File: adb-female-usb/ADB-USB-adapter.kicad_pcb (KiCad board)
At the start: 2 copper layers, 31.8 x 21.6 mm, 2 parts

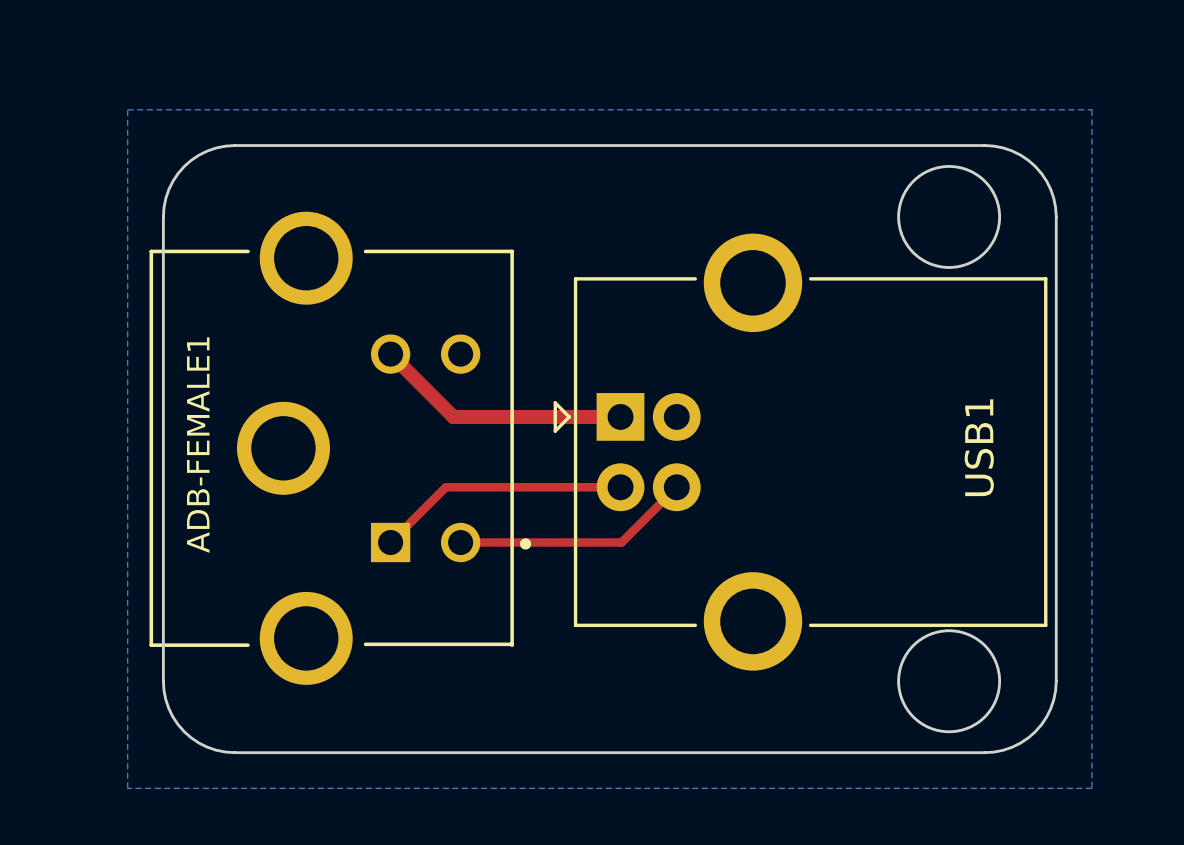
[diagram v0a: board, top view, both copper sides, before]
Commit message: switched D+/D- on USB PCB, isolated shield from ground
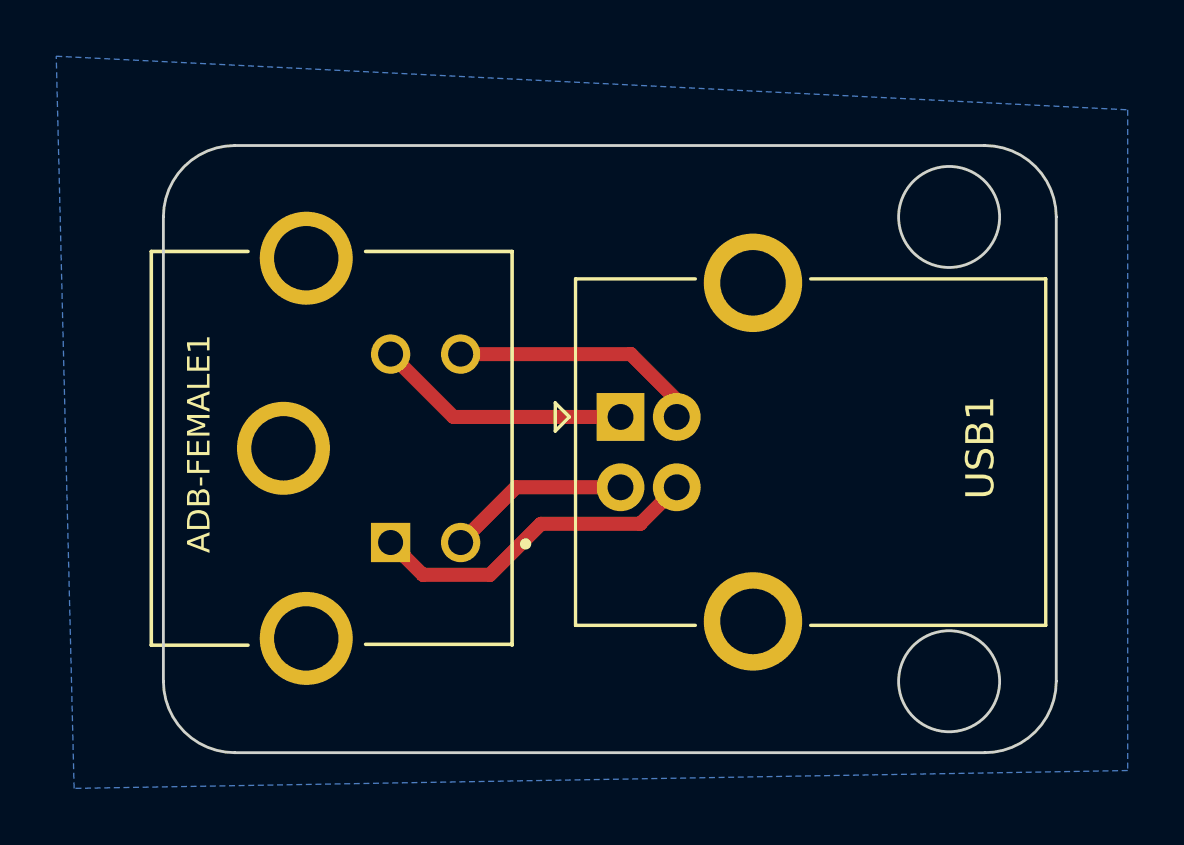
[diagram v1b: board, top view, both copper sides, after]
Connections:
- ADB-FEMALE1 pad 1: Net-(USB1-D-) -> Net-(USB1-D+)
- ADB-FEMALE1 pad 3: Net-(USB1-D+) -> Net-(USB1-D-)
- ADB-FEMALE1 pad 5: GND -> Net-(USB1-Shield)
- ADB-FEMALE1 pad 6: GND -> Net-(USB1-Shield)
- ADB-FEMALE1 pad 7: GND -> Net-(USB1-Shield)
- USB1 pad 5: GND -> Net-(USB1-Shield)
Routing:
- net GND: track 0.00 -> 8.96 mm
- net Net-(USB1-D+): track 8.50 -> 11.9 mm
- net Net-(USB1-D-): track 8.99 -> 6.50 mm
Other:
- board text added: "joanne-lab rev 2.0"
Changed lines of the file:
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@@
       (outputformat 1)
       (mirror false)
-      (drillshape 1)
+      (drillshape 0)
       (scaleselection 1)
-      (outputdirectory "")
+      (outputdirectory "../fabrication/adb-female-usb/")
     )
   )
   (net 0 "")
-  (net 1 "GND")
-  (net 2 "Net-(USB1-VBUS)")
-  (net 3 "Net-(USB1-D+)")
-  (net 4 "Net-(USB1-D-)")
+  (net 1 "Net-(USB1-VBUS)")
+  (net 2 "Net-(USB1-D+)")
+  (net 3 "Net-(USB1-D-)")
+  (net 4 "Net-(USB1-Shield)")
+  (net 5 "GND")
   (footprint "Connector_USB:USB_B_OST_USB-B1HSxx_Horizontal" (layer "F.Cu")
     (at 36.576 28.702)
@@
       (stroke (width 0.1) (type solid)) (layer "F.Fab"))
     (pad "1" thru_hole rect (at 0 0) (size 1.7 1.7) (drill 0.92) (layers "*.Cu" "*.Mask")
-      (net 2 "Net-(USB1-VBUS)") (pinfunction "VBUS") (pintype "power_out"))
+      (net 1 "Net-(USB1-VBUS)") (pinfunction "VBUS") (pintype "power_out"))
     (pad "2" thru_hole circle (at 0 2.5) (size 1.7 1.7) (drill 0.92) (layers "*.Cu" "*.Mask")
-      (net 4 "Net-(USB1-D-)") (pinfunction "D-") (pintype "bidirectional"))
+      (net 3 "Net-(USB1-D-)") (pinfunction "D-") (pintype "bidirectional"))
     (pad "3" thru_hole circle (at 2 2.5) (size 1.7 1.7) (drill 0.92) (layers "*.Cu" "*.Mask")
-      (net 3 "Net-(USB1-D+)") (pinfunction "D+") (pintype "bidirectional"))
+      (net 2 "Net-(USB1-D+)") (pinfunction "D+") (pintype "bidirectional"))
     (pad "4" thru_hole circle (at 2 0) (size 1.7 1.7) (drill 0.92) (layers "*.Cu" "*.Mask")
-      (net 1 "GND") (pinfunction "GND") (pintype "power_out"))
+      (net 5 "GND") (pinfunction "GND") (pintype "power_out"))
     (pad "5" thru_hole circle (at 4.71 -4.77) (size 3.5 3.5) (drill 2.33) (layers "*.Cu" "*.Mask")
-      (net 1 "GND") (pinfunction "Shield") (pintype "passive"))
+      (net 4 "Net-(USB1-Shield)") (pinfunction "Shield") (pintype "passive"))
     (pad "5" thru_hole circle (at 4.71 7.27) (size 3.5 3.5) (drill 2.33) (layers "*.Cu" "*.Mask")
-      (net 1 "GND") (pinfunction "Shield") (pintype "passive"))
+      (net 4 "Net-(USB1-Shield)") (pinfunction "Shield") (pintype "passive"))
     (model "${KICAD6_3DMODEL_DIR}/Connector_USB.3dshapes/USB_B_OST_USB-B1HSxx_Horizontal.wrl"
       (offset (xyz 0 0 0))
@@
       (stroke (width 0.127) (type solid)) (layer "F.Fab"))
     (pad "1" thru_hole rect (at -3.35 0 90) (size 1.398 1.398) (drill 0.89) (layers "*.Cu" "*.Mask")
-      (net 4 "Net-(USB1-D-)") (pinfunction "1") (pintype "passive") (solder_mask_margin 0.102))
+      (net 2 "Net-(USB1-D+)") (pinfunction "1") (pintype "passive") (solder_mask_margin 0.102))
     (pad "2" thru_hole circle (at 3.35 0 90) (size 1.398 1.398) (drill 0.89) (layers "*.Cu" "*.Mask")
-      (net 2 "Net-(USB1-VBUS)") (pinfunction "2") (pintype "passive") (solder_mask_margin 0.102))
+      (net 1 "Net-(USB1-VBUS)") (pinfunction "2") (pintype "passive") (solder_mask_margin 0.102))
     (pad "3" thru_hole circle (at -3.35 2.49 90) (size 1.398 1.398) (drill 0.89) (layers "*.Cu" "*.Mask")
-      (net 3 "Net-(USB1-D+)") (pinfunction "3") (pintype "passive") (solder_mask_margin 0.102))
+      (net 3 "Net-(USB1-D-)") (pinfunction "3") (pintype "passive") (solder_mask_margin 0.102))
     (pad "4" thru_hole circle (at 3.35 2.49 90) (size 1.398 1.398) (drill 0.89) (layers "*.Cu" "*.Mask")
-      (net 1 "GND") (pinfunction "4") (pintype "passive") (solder_mask_margin 0.102))
+      (net 5 "GND") (pinfunction "4") (pintype "passive") (solder_mask_margin 0.102))
     (pad "5" thru_hole circle (at 0 -3.81 90) (size 3.306 3.306) (drill 2.29) (layers "*.Cu" "*.Mask")
-      (net 1 "GND") (pinfunction "SH") (pintype "passive") (solder_mask_margin 0.102))
+      (net 4 "Net-(USB1-Shield)") (pinfunction "SH") (pintype "passive") (solder_mask_margin 0.102))
     (pad "6" thru_hole circle (at 6.76 -3 90) (size 3.306 3.306) (drill 2.29) (layers "*.Cu" "*.Mask")
-      (net 1 "GND") (pinfunction "SH") (pintype "passive") (solder_mask_margin 0.102))
+      (net 4 "Net-(USB1-Shield)") (pinfunction "SH") (pintype "passive") (solder_mask_margin 0.102))
     (pad "7" thru_hole circle (at -6.76 -3 90) (size 3.306 3.306) (drill 2.29) (layers "*.Cu" "*.Mask")
-      (net 1 "GND") (pinfunction "SH") (pintype "passive") (solder_mask_margin 0.102))
+      (net 4 "Net-(USB1-Shield)") (pinfunction "SH") (pintype "passive") (solder_mask_margin 0.102))
   )
   (gr_circle (center 48.26 38.1) (end 49.53 39.37)
@@
   (gr_line (start 22.86 19.05) (end 49.53 19.05)
     (stroke (width 0.1) (type default)) (layer "Edge.Cuts"))
+  (gr_text "joanne-lab\nrev 2.0" (at 49.53 31.115) (layer "B.SilkS")
+    (effects (font (size 1 1) (thickness 0.15)) (justify left bottom mirror))
+  )
   (gr_text "GND" (at 30.226 25.4 -90) (layer "B.SilkS")
     (effects (font (size 1 1) (thickness 0.15)) (justify left bottom mirror))
@@
     (effects (font (size 1 1) (thickness 0.15)) (justify left bottom mirror))
   )
-  (segment (start 28.4 26.4668) (end 30.6352 28.702) (width 0.5) (layer "F.Cu") (net 2))
-  (segment (start 30.6352 28.702) (end 36.576 28.702) (width 0.5) (layer "F.Cu") (net 2))
-  (segment (start 36.6112 33.1668) (end 30.89 33.1668) (width 0.3) (layer "F.Cu") (net 3))
-  (segment (start 38.576 31.202) (end 36.6112 33.1668) (width 0.3) (layer "F.Cu") (net 3))
-  (segment (start 36.576 31.202) (end 30.3648 31.202) (width 0.3) (layer "F.Cu") (net 4))
-  (segment (start 30.3648 31.202) (end 28.4 33.1668) (width 0.3) (layer "F.Cu") (net 4))
-  (zone (net 1) (net_name "GND") (layer "B.Cu") (hatch edge 0.5)
+  (segment (start 36.576 28.702) (end 30.6352 28.702) (width 0.5) (layer "F.Cu") (net 1))
+  (segment (start 30.6352 28.702) (end 28.4 26.4668) (width 0.5) (layer "F.Cu") (net 1))
+  (segment (start 31.93095 34.3158) (end 29.549 34.3158) (width 0.5) (layer "F.Cu") (net 2))
+  (segment (start 29.549 34.3158) (end 28.4 33.1668) (width 0.5) (layer "F.Cu") (net 2))
+  (segment (start 33.74475 32.502) (end 31.93095 34.3158) (width 0.5) (layer "F.Cu") (net 2))
+  (segment (start 37.276 32.502) (end 33.74475 32.502) (width 0.5) (layer "F.Cu") (net 2))
+  (segment (start 38.576 31.202) (end 37.276 32.502) (width 0.5) (layer "F.Cu") (net 2))
+  (segment (start 32.8548 31.202) (end 30.89 33.1668) (width 0.5) (layer "F.Cu") (net 3))
+  (segment (start 36.576 31.202) (end 32.8548 31.202) (width 0.5) (layer "F.Cu") (net 3))
+  (segment (start 36.9408 26.4668) (end 30.89 26.4668) (width 0.5) (layer "F.Cu") (net 5))
+  (segment (start 38.576 28.102) (end 36.9408 26.4668) (width 0.5) (layer "F.Cu") (net 5))
+  (segment (start 38.576 28.702) (end 38.576 28.102) (width 0.5) (layer "F.Cu") (net 5))
+  (zone (net 5) (net_name "GND") (layer "B.Cu") (hatch edge 0.5)
     (connect_pads (clearance 0.5))
     (min_thickness 0.25) (filled_areas_thickness no)
@@
     (polygon
       (pts
-        (xy 53.34 17.78)
-        (xy 53.34 41.91)
-        (xy 19.05 41.91)
-        (xy 19.05 17.78)
+        (xy 54.61 17.78)
+        (xy 54.61 41.275)
+        (xy 17.145 41.91)
+        (xy 16.51 15.875)
       )
     )
